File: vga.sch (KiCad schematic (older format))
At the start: 1 part

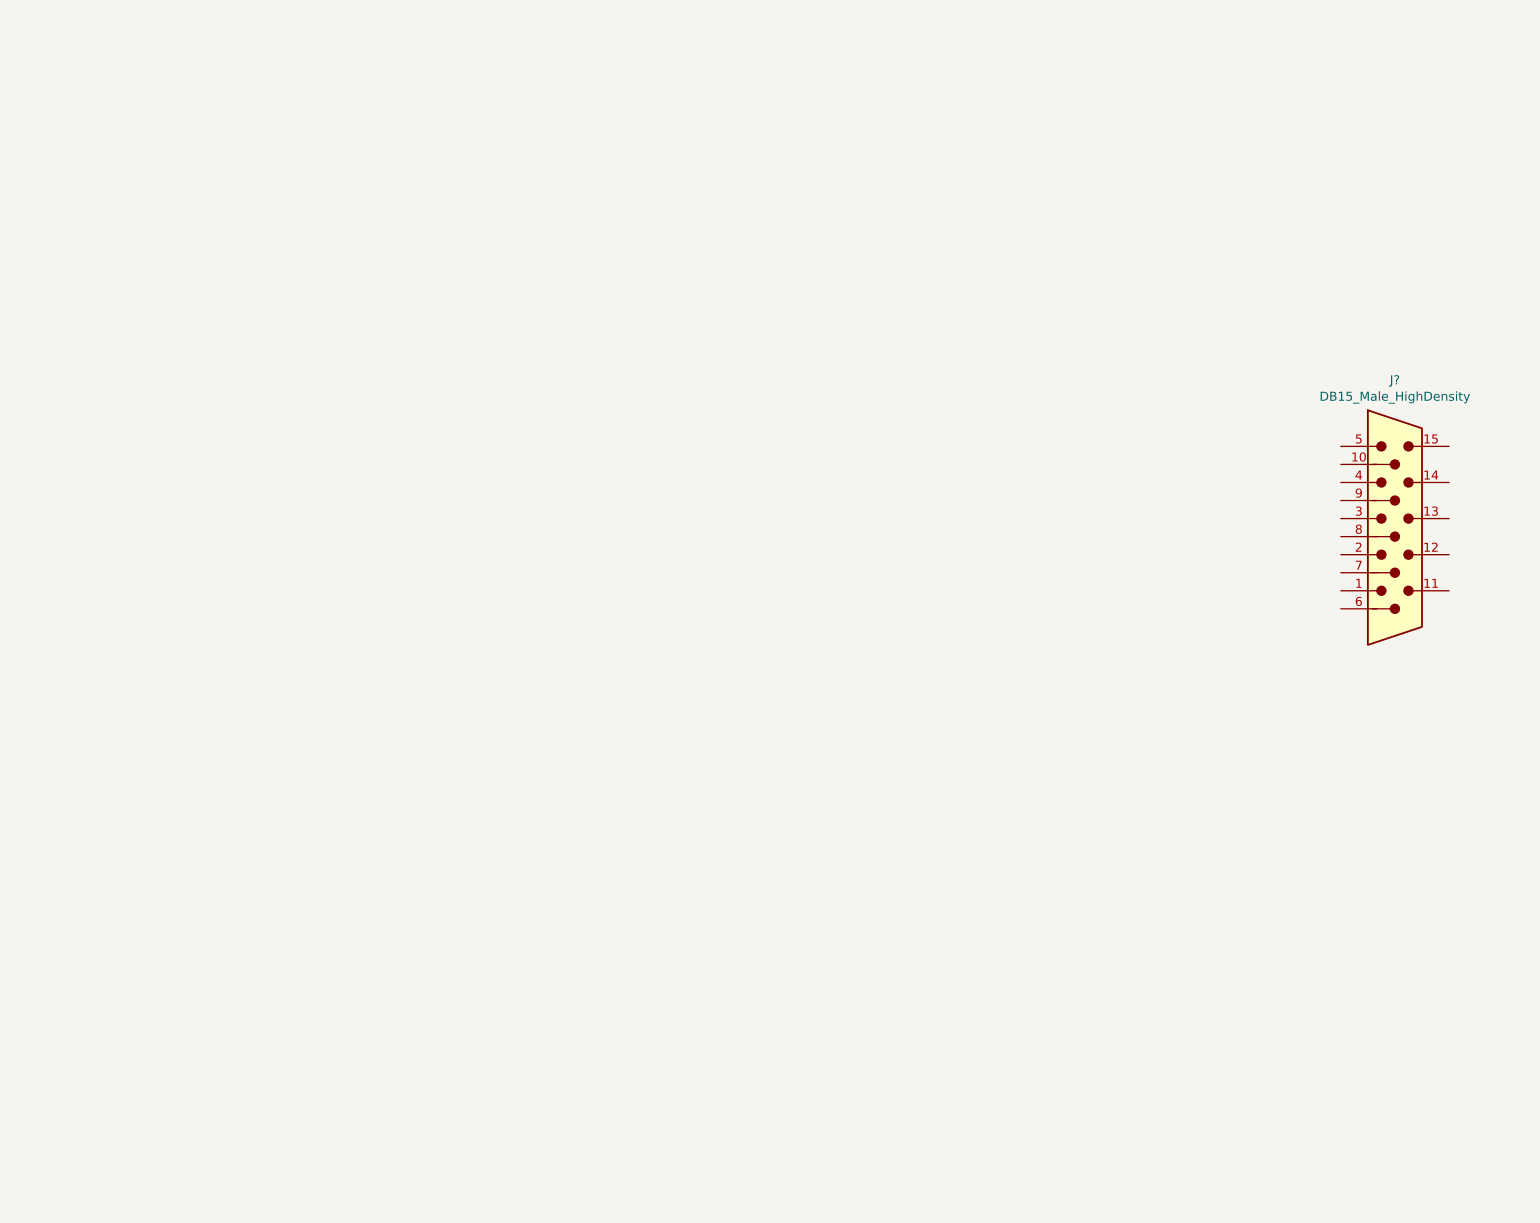
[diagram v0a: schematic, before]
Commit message: HDMI and VGA circuit added.
Signed-off-by: Kali Prasad <kprasadvnsi@protonmail.com>
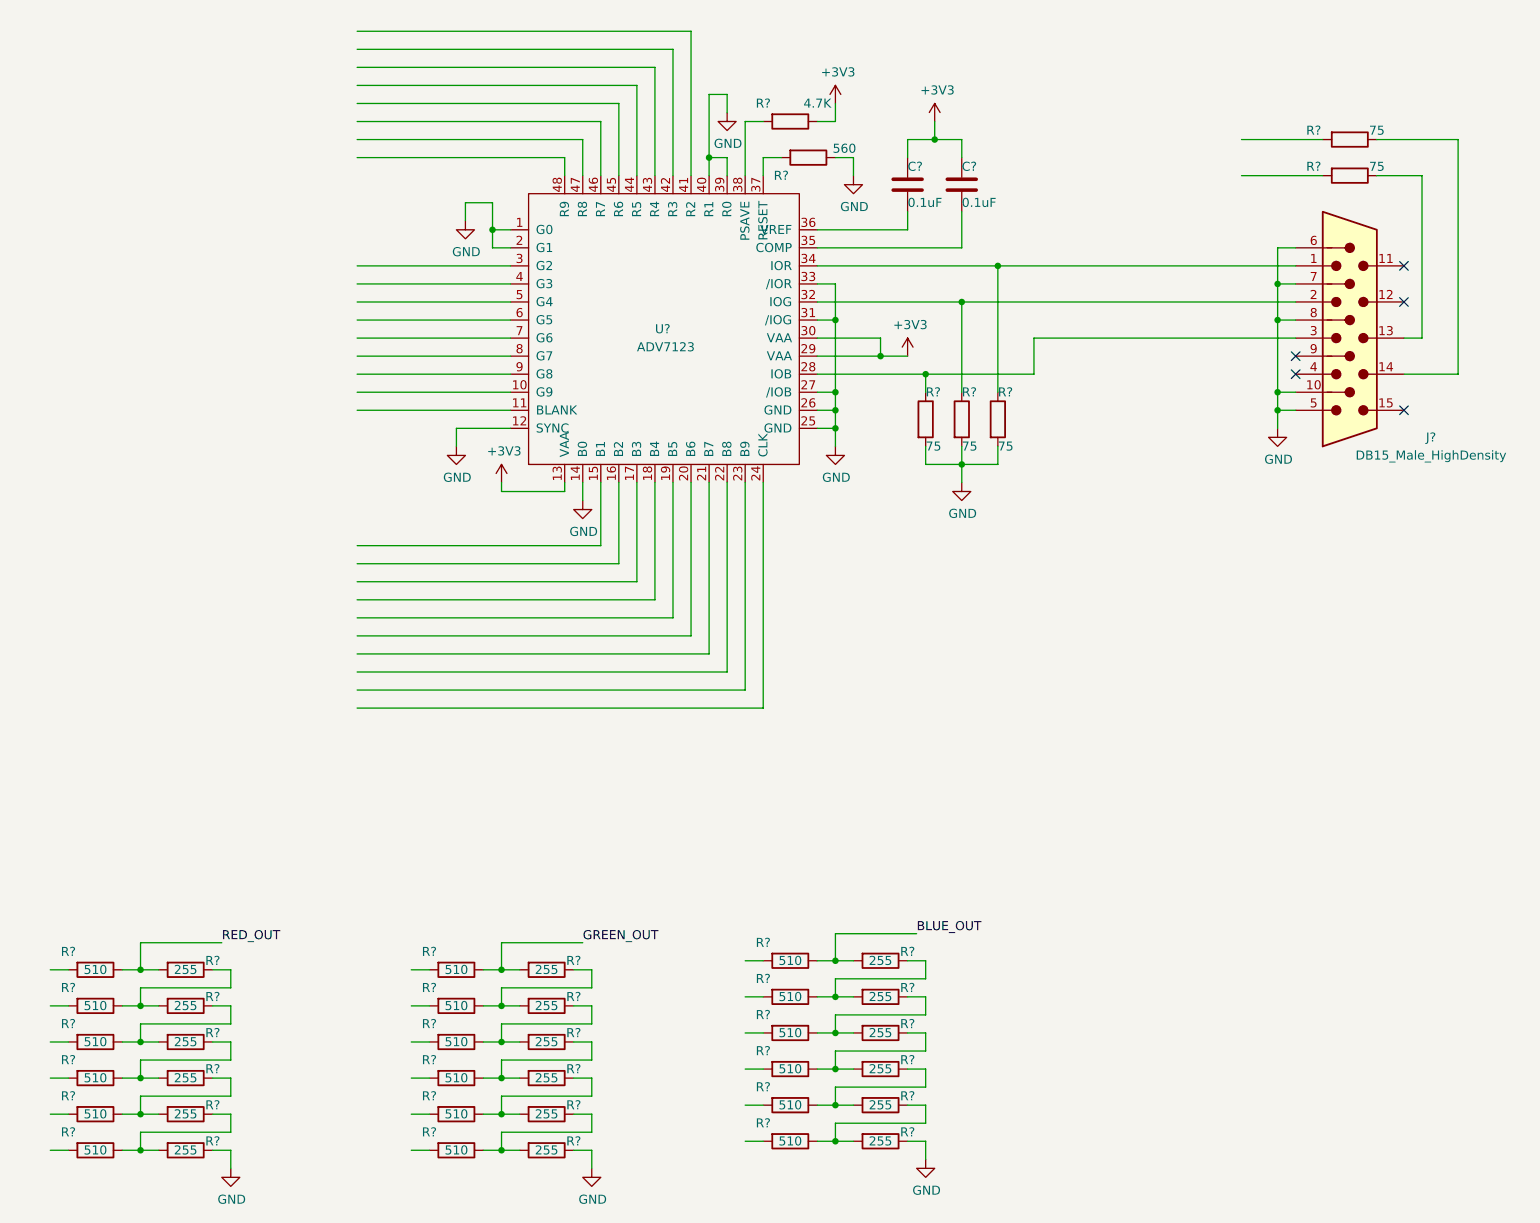
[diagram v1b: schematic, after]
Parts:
- added C? (x2): 0.1uF, symbol Device:C
- added R? (x18): 510, symbol Device:R
- added R? (x18): 255, symbol Device:R
- added R?: 4.7K, symbol Device:R
- added R?: 560, symbol Device:R
- added R? (x5): 75, symbol Device:R
- added U?: ADV7123, Package_QFP:LQFP-48_7x7mm_P0.5mm, symbol lt_eval_board:ADV7123
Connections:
- net labels added: +3V3, BLUE_OUT, GND, GREEN_OUT, RED_OUT
- wire segments 0 -> 255
- no-connect marks 0 -> 5
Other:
- moved on the sheet: J?

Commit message: SOM added.
Signed-off-by: Kali Prasad <kprasadvnsi@protonmail.com>
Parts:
- C1, C2: renamed from C?; footprint (none) -> Capacitor_SMD:C_0805_2012Metric_Pad1.15x1.40mm_HandSolder
- J3: renamed from J?; footprint (none) -> Connector_Dsub:DSUB-15-HD_Female_Horizontal_P2.29x1.98mm_EdgePinOffset3.03mm_Housed_MountingHolesOffset4.94mm
- R1, R10, R11, R12, R13, R14, R15, R16, R17, R18, R19, R2, R20, R21, R22, R23, R24, R25, R26, R27, R28, R29, R3, R30, R31, R32, R33, R34, R35, R36, R37, R38, R39, R4, R40, R41, R42, R43, R5, R6, R7, R8, R9: renamed from R?; footprint (none) -> Resistor_SMD:R_0805_2012Metric_Pad1.15x1.40mm_HandSolder
- gave numbers to parts that had none: 1
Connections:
- net labels added: B0, B1, B2, B3, B4, B5, B6, B7, BLUE_0, BLUE_1, BLUE_2, BLUE_3, BLUE_4, BLUE_5, BLUE_6, BLUE_7, G0, G1, G2, G3, G4, G5, G6, G7, GREEN_0, GREEN_1, GREEN_2, GREEN_3, GREEN_4, GREEN_5, GREEN_6, GREEN_7, R0, R1, R2, R3, R4, R5, R6, R7, RED_0, RED_1, RED_2, RED_3, RED_4, RED_5, RED_6, RED_7, VGA_CLK, VGA_CLOCK, VGA_HS, VGA_VS
- wire segments 255 -> 259
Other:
- moved on the sheet: R26, R27, R28, R29, R30, R31, R33, R34, R35, R36, R37, R38
